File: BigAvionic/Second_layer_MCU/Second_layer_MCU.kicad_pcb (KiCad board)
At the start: 4 copper layers, 68 x 68 mm, 89 parts, among them J1 Conn_01x02, J10 Conn_01x04, J12 Conn_01x04, J2 USB_C_Receptacle_USB2.0_16P, J3 Conn_01x04, J6 Micro_SD_Card_Det1, J7 Screw_Terminal_01x01, J9 Conn_01x04, Q5 NMOS, SW1 SW_Push, SW2 USER_Buttom, SW3 USER_Buttom, U1 STM32F405VGTx, U12 W25Q128JVS, U5 BMI088, U6 BMP390, U8 ADXL375BCCZ, Y1 8Mhz

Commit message: finish power layer(still need check)
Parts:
- removed J7: Screw_Terminal_01x01, TerminalBlock_Phoenix:TerminalBlock_Phoenix_PT-1,5-2-3.5-H_1x02_P3.50mm_Horizontal
- removed R10: 0 ohm, Resistor_SMD:R_0805_2012Metric_Pad1.20x1.40mm_HandSolder
- removed R5, R54: 0ohm, Resistor_SMD:R_0805_2012Metric_Pad1.20x1.40mm_HandSolder
- added J4: Screw_Terminal_01x02, TerminalBlock_Phoenix:TerminalBlock_Phoenix_PT-1,5-2-3.5-H_1x02_P3.50mm_Horizontal, F.Cu at (86.1, 67.9)
- C1, C11, C2, C20, C25, C26, C27, C28, C29, C3, C30, C31, C32, C36, C37, C4, C48, C5, C50, C51, C53, C6, C7, C8, C9: footprint Capacitor_SMD:C_0805_2012Metric_Pad1.18x1.45mm_HandSolder -> Capacitor_SMD:C_0603_1608Metric_Pad1.08x0.95mm_HandSolder
- R35, R38, R40, R41, R44: value 47k -> 10k
- Y1: footprint Crystal:Crystal_HC49-U_Vertical -> Crystal:Crystal_SMD_5032-4Pin_5.0x3.2mm
- moved U1 91.3 mm to (130.5, 120.0)
- moved D11 62.0 mm to (84.0, 33.5)
- moved D12 62.0 mm to (84.0, 36.6)
- moved D5 62.0 mm to (84.0, 27.4)
- moved BZ1 62.0 mm to (71.0, 32.7)
- moved D8 62.0 mm to (84.0, 30.5)
- moved U6 48.8 mm to (43.5, 81.6)
- moved Q5 48.8 mm to (38.9, 81.7)
- moved U5 48.8 mm to (33.4, 82.2)
- moved J12 47.0 mm to (33.8, 76.2)
- moved J6 27.4 mm to (68.4, 73.2)
- moved U12 26.4 mm to (82.0, 78.6)
- moved C11 23.3 mm to (37.5, 33.4)
- moved C27 23.3 mm to (37.5, 45.5)
- moved C3 23.3 mm to (32.6, 33.4)
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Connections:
- C28 pad 1: Net-(C28-Pad1) -> HSE_OUT
- J2 pad A6: Net-(J2-D+-PadA6) -> USB_D+
- J2 pad A7: Net-(J2-D--PadA7) -> USB_D-
- J2 pad B6: Net-(J2-D+-PadA6) -> USB_D+
- J2 pad B7: Net-(J2-D--PadA7) -> USB_D-
- R39 pad 2: SDIO_CK -> SDIO_CMD

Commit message: add lora files
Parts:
- added J5: Conn_01x08, Connector_JST:JST_GH_SM08B-GHS-TB_1x08-1MP_P1.25mm_Horizontal, B.Cu at (160.5, 110.0)
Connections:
- net +USB_5V renamed Net-(J2-VBUS-PadA4)
- U1 pad 16: unconnected-(U1-PC1-Pad16) -> SUP_STAT
- U1 pad 17: unconnected-(U1-PC2-Pad17) -> PG_BUCK

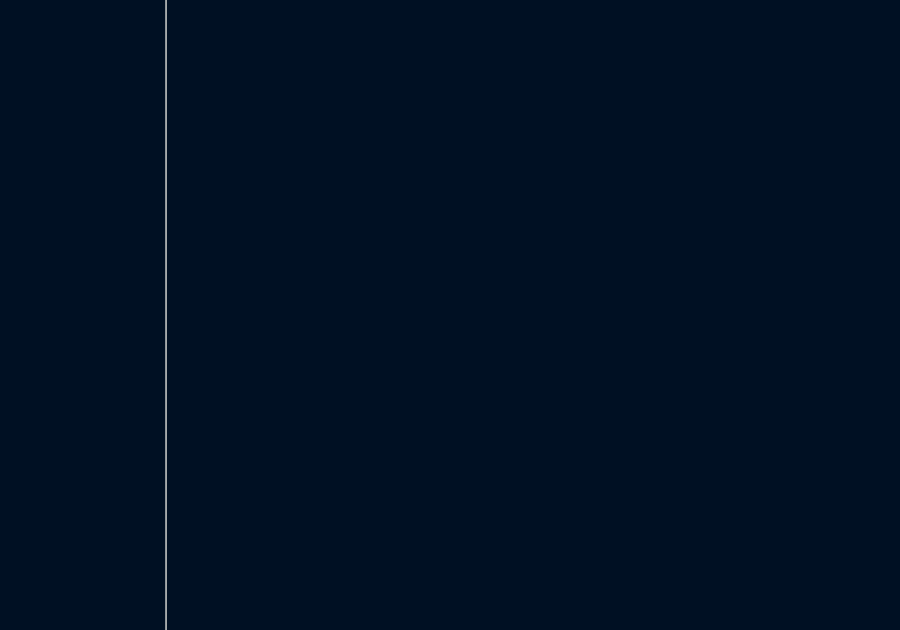
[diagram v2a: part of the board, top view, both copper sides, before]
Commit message: add new power layer
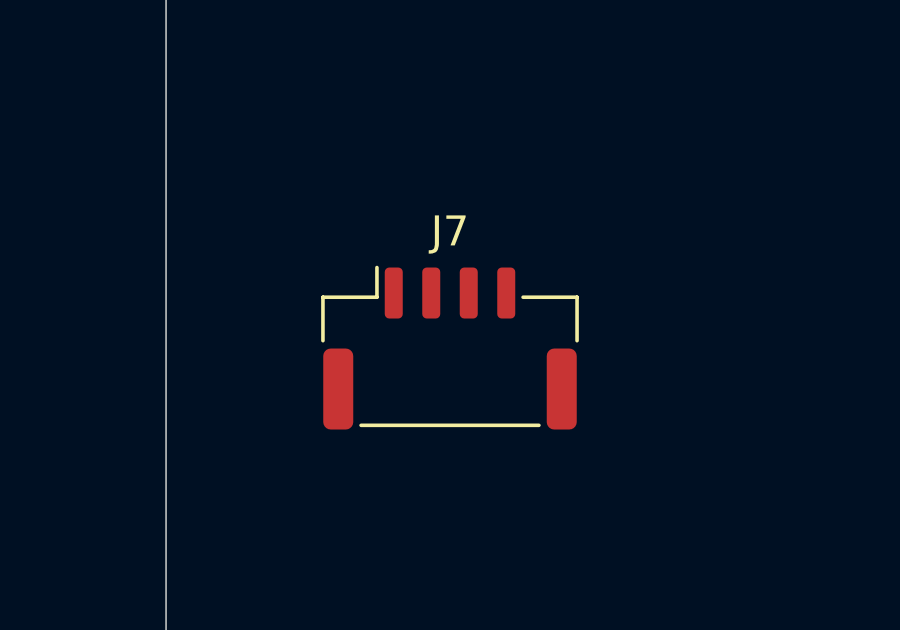
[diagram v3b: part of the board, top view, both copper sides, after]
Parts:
- added J7: Conn_01x04, Connector_JST:JST_GH_SM04B-GHS-TB_1x04-1MP_P1.25mm_Horizontal, F.Cu at (106.0, 123.8)

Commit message: MCU process
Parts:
- removed Q5: NMOS, Package_TO_SOT_SMD:SOT-23
- removed the R27 at (37.4, 54.4)
- removed R34, R36, R37, R39, R42, R43: 22ohm, Resistor_SMD:R_0805_2012Metric_Pad1.20x1.40mm_HandSolder
- added C30: 22u, Capacitor_SMD:C_1206_3216Metric_Pad1.33x1.80mm_HandSolder, B.Cu at (154.5, 110.1)
- added C31: 22u, Capacitor_SMD:C_1206_3216Metric_Pad1.33x1.80mm_HandSolder, B.Cu at (150.8, 110.1)
- added J11: Conn_01x04, Connector_JST:JST_GH_SM04B-GHS-TB_1x04-1MP_P1.25mm_Horizontal, B.Cu at (160.5, 110.1)
- added J13: Conn_01x08, Connector_JST:JST_GH_SM08B-GHS-TB_1x08-1MP_P1.25mm_Horizontal, F.Cu at (120.5, 90.0)
- added J14: Conn_01x08, Connector_JST:JST_GH_SM08B-GHS-TB_1x08-1MP_P1.25mm_Horizontal, F.Cu at (140.5, 90.0)
- added Q2: BSS138, Package_TO_SOT_SMD:SOT-23, F.Cu at (131.3, 78.5)
- added R1: 100k, Resistor_SMD:R_0402_1005Metric_Pad0.72x0.64mm_HandSolder, F.Cu at (125.0, 67.5)
- added R17: 22ohm, Resistor_SMD:R_0402_1005Metric_Pad0.72x0.64mm_HandSolder, F.Cu at (141.3, 124.0)
- added R19: 22ohm, Resistor_SMD:R_0402_1005Metric_Pad0.72x0.64mm_HandSolder, F.Cu at (133.2, 109.4)
- added R32: 22ohm, Resistor_SMD:R_0402_1005Metric_Pad0.72x0.64mm_HandSolder, F.Cu at (133.7, 70.0)
- added R33: 22ohm, Resistor_SMD:R_0402_1005Metric_Pad0.72x0.64mm_HandSolder, B.Cu at (133.1, 109.4)
- added R35: 10k, Resistor_SMD:R_0402_1005Metric_Pad0.72x0.64mm_HandSolder, F.Cu at (107.8, 132.6)
- added R4: 4.7k, Resistor_SMD:R_0402_1005Metric_Pad0.72x0.64mm_HandSolder, F.Cu at (125.0, 70.0)
- added R5: 4.7k, Resistor_SMD:R_0402_1005Metric_Pad0.72x0.64mm_HandSolder, F.Cu at (125.0, 72.5)
- added R6: 22ohm, Resistor_SMD:R_0402_1005Metric_Pad0.72x0.64mm_HandSolder, F.Cu at (141.4, 119.0)
- added R7: 22ohm, Resistor_SMD:R_0402_1005Metric_Pad0.72x0.64mm_HandSolder, F.Cu at (141.3, 117.8)
- added R8: 22ohm, Resistor_SMD:R_0402_1005Metric_Pad0.72x0.64mm_HandSolder, F.Cu at (135.6, 109.4)
- added R9: 22ohm, Resistor_SMD:R_0402_1005Metric_Pad0.72x0.64mm_HandSolder, F.Cu at (134.4, 109.4)
- BZ1: footprint Buzzer_Beeper:Buzzer_12x9.5RM7.6 -> Buzzer_Beeper:MagneticBuzzer_CUI_CMT-8504-100-SMT
- C10: renamed from C8; footprint Capacitor_SMD:C_0603_1608Metric_Pad1.08x0.95mm_HandSolder -> Capacitor_SMD:C_0402_1005Metric_Pad0.74x0.62mm_HandSolder
- C11: renamed from C9; footprint Capacitor_SMD:C_0603_1608Metric_Pad1.08x0.95mm_HandSolder -> Capacitor_SMD:C_0402_1005Metric_Pad0.74x0.62mm_HandSolder
- C13: renamed from C48; footprint Capacitor_SMD:C_0603_1608Metric_Pad1.08x0.95mm_HandSolder -> Capacitor_SMD:C_0402_1005Metric_Pad0.74x0.62mm_HandSolder
- C14: renamed from C20; footprint Capacitor_SMD:C_0603_1608Metric_Pad1.08x0.95mm_HandSolder -> Capacitor_SMD:C_0402_1005Metric_Pad0.74x0.62mm_HandSolder
- C15: renamed from C25; footprint Capacitor_SMD:C_0603_1608Metric_Pad1.08x0.95mm_HandSolder -> Capacitor_SMD:C_0402_1005Metric_Pad0.74x0.62mm_HandSolder
- C16: renamed from C11; footprint Capacitor_SMD:C_0603_1608Metric_Pad1.08x0.95mm_HandSolder -> Capacitor_SMD:C_0402_1005Metric_Pad0.74x0.62mm_HandSolder
- C2: renamed from C3; footprint Capacitor_SMD:C_0603_1608Metric_Pad1.08x0.95mm_HandSolder -> Capacitor_SMD:C_0402_1005Metric_Pad0.74x0.62mm_HandSolder
- C20: renamed from C36; footprint Capacitor_SMD:C_0603_1608Metric_Pad1.08x0.95mm_HandSolder -> Capacitor_SMD:C_0402_1005Metric_Pad0.74x0.62mm_HandSolder
- C22: renamed from C37; footprint Capacitor_SMD:C_0603_1608Metric_Pad1.08x0.95mm_HandSolder -> Capacitor_SMD:C_0402_1005Metric_Pad0.74x0.62mm_HandSolder
- C23: renamed from C29; footprint Capacitor_SMD:C_0603_1608Metric_Pad1.08x0.95mm_HandSolder -> Capacitor_SMD:C_0402_1005Metric_Pad0.74x0.62mm_HandSolder
- C24: renamed from C50; footprint Capacitor_SMD:C_0603_1608Metric_Pad1.08x0.95mm_HandSolder -> Capacitor_SMD:C_0402_1005Metric_Pad0.74x0.62mm_HandSolder
- C25: renamed from C30; footprint Capacitor_SMD:C_0603_1608Metric_Pad1.08x0.95mm_HandSolder -> Capacitor_SMD:C_0402_1005Metric_Pad0.74x0.62mm_HandSolder
- C26: renamed from C31; footprint Capacitor_SMD:C_0603_1608Metric_Pad1.08x0.95mm_HandSolder -> Capacitor_SMD:C_0402_1005Metric_Pad0.74x0.62mm_HandSolder
- C27: renamed from C32; footprint Capacitor_SMD:C_0603_1608Metric_Pad1.08x0.95mm_HandSolder -> Capacitor_SMD:C_0402_1005Metric_Pad0.74x0.62mm_HandSolder
- C28: renamed from C51; footprint Capacitor_SMD:C_0603_1608Metric_Pad1.08x0.95mm_HandSolder -> Capacitor_SMD:C_0402_1005Metric_Pad0.74x0.62mm_HandSolder
- C29: renamed from C53; footprint Capacitor_SMD:C_0603_1608Metric_Pad1.08x0.95mm_HandSolder -> Capacitor_SMD:C_0402_1005Metric_Pad0.74x0.62mm_HandSolder
- C3: renamed from C26; footprint Capacitor_SMD:C_0603_1608Metric_Pad1.08x0.95mm_HandSolder -> Capacitor_SMD:C_0402_1005Metric_Pad0.74x0.62mm_HandSolder
- C4, C5, C6, C7: footprint Capacitor_SMD:C_0603_1608Metric_Pad1.08x0.95mm_HandSolder -> Capacitor_SMD:C_0402_1005Metric_Pad0.74x0.62mm_HandSolder
- D4: renamed from D12; footprint LED_SMD:LED_0805_2012Metric_Pad1.15x1.40mm_HandSolder -> Diode_SMD:D_SOD-123
- J10: renamed from J7; moved to B.Cu
- J4: renamed from J6; footprint Connector_Card:microSD_HC_Molex_47219-2001 -> Connector_Card:microSD_HC_Molex_104031-0811
- J5: renamed from J10; footprint Connector_JST:JST_EH_S4B-EH_1x04_P2.50mm_Horizontal -> Connector_JST:JST_GH_SM04B-GHS-TB_1x04-1MP_P1.25mm_Horizontal
- J6: renamed from J12; footprint Connector_JST:JST_EH_B4B-EH-A_1x04_P2.50mm_Vertical -> Connector_PinHeader_2.54mm:PinHeader_1x04_P2.54mm_Vertical
- J8: renamed from J9; footprint Connector_JST:JST_EH_S4B-EH_1x04_P2.50mm_Horizontal -> Connector_JST:JST_GH_SM04B-GHS-TB_1x04-1MP_P1.25mm_Horizontal
- J9: renamed from J5; moved to F.Cu
- R10: renamed from R44; footprint Resistor_SMD:R_0805_2012Metric_Pad1.20x1.40mm_HandSolder -> Resistor_SMD:R_0402_1005Metric_Pad0.72x0.64mm_HandSolder; moved to B.Cu
- R11: renamed from R40; footprint Resistor_SMD:R_0805_2012Metric_Pad1.20x1.40mm_HandSolder -> Resistor_SMD:R_0402_1005Metric_Pad0.72x0.64mm_HandSolder; moved to B.Cu
- R12: renamed from R9; footprint Resistor_SMD:R_0805_2012Metric_Pad1.20x1.40mm_HandSolder -> Resistor_SMD:R_0402_1005Metric_Pad0.72x0.64mm_HandSolder
- R13: renamed from R38; footprint Resistor_SMD:R_0805_2012Metric_Pad1.20x1.40mm_HandSolder -> Resistor_SMD:R_0402_1005Metric_Pad0.72x0.64mm_HandSolder; moved to B.Cu
- R14: renamed from R41; footprint Resistor_SMD:R_0805_2012Metric_Pad1.20x1.40mm_HandSolder -> Resistor_SMD:R_0402_1005Metric_Pad0.72x0.64mm_HandSolder; moved to B.Cu
- R15: renamed from R35; footprint Resistor_SMD:R_0805_2012Metric_Pad1.20x1.40mm_HandSolder -> Resistor_SMD:R_0402_1005Metric_Pad0.72x0.64mm_HandSolder; moved to B.Cu
- R16: renamed from R3; footprint Resistor_SMD:R_0805_2012Metric_Pad1.20x1.40mm_HandSolder -> Resistor_SMD:R_0402_1005Metric_Pad0.72x0.64mm_HandSolder
- R18: renamed from R4; footprint Resistor_SMD:R_0805_2012Metric_Pad1.20x1.40mm_HandSolder -> Resistor_SMD:R_0402_1005Metric_Pad0.72x0.64mm_HandSolder
- R2: renamed from R6; footprint Resistor_SMD:R_0805_2012Metric_Pad1.20x1.40mm_HandSolder -> Resistor_SMD:R_0402_1005Metric_Pad0.72x0.64mm_HandSolder
- R20: renamed from R45; footprint Resistor_SMD:R_0805_2012Metric_Pad1.20x1.40mm_HandSolder -> Resistor_SMD:R_0402_1005Metric_Pad0.72x0.64mm_HandSolder
- R21: renamed from R46; footprint Resistor_SMD:R_0805_2012Metric_Pad1.20x1.40mm_HandSolder -> Resistor_SMD:R_0402_1005Metric_Pad0.72x0.64mm_HandSolder
- R22: renamed from R47; footprint Resistor_SMD:R_0805_2012Metric_Pad1.20x1.40mm_HandSolder -> Resistor_SMD:R_0402_1005Metric_Pad0.72x0.64mm_HandSolder
- R23: footprint Resistor_SMD:R_0805_2012Metric_Pad1.20x1.40mm_HandSolder -> Resistor_SMD:R_0402_1005Metric_Pad0.72x0.64mm_HandSolder
- R24: renamed from R8; footprint Resistor_SMD:R_0805_2012Metric_Pad1.20x1.40mm_HandSolder -> Resistor_SMD:R_0402_1005Metric_Pad0.72x0.64mm_HandSolder
- R25: renamed from R22; footprint Resistor_SMD:R_0805_2012Metric_Pad1.20x1.40mm_HandSolder -> Resistor_SMD:R_0402_1005Metric_Pad0.72x0.64mm_HandSolder
- R26: renamed from R28; footprint Resistor_SMD:R_0805_2012Metric_Pad1.20x1.40mm_HandSolder -> Resistor_SMD:R_0402_1005Metric_Pad0.72x0.64mm_HandSolder
- R27: renamed from R48; footprint Resistor_SMD:R_0805_2012Metric_Pad1.20x1.40mm_HandSolder -> Resistor_SMD:R_0402_1005Metric_Pad0.72x0.64mm_HandSolder
- R28: renamed from R49; footprint Resistor_SMD:R_0805_2012Metric_Pad1.20x1.40mm_HandSolder -> Resistor_SMD:R_0402_1005Metric_Pad0.72x0.64mm_HandSolder
- R29: renamed from R53; footprint Resistor_SMD:R_0805_2012Metric_Pad1.20x1.40mm_HandSolder -> Resistor_SMD:R_0402_1005Metric_Pad0.72x0.64mm_HandSolder
- R3: renamed from R7; footprint Resistor_SMD:R_0805_2012Metric_Pad1.20x1.40mm_HandSolder -> Resistor_SMD:R_0402_1005Metric_Pad0.72x0.64mm_HandSolder
- R30: renamed from R50; footprint Resistor_SMD:R_0805_2012Metric_Pad1.20x1.40mm_HandSolder -> Resistor_SMD:R_0402_1005Metric_Pad0.72x0.64mm_HandSolder
- R31: renamed from R51; footprint Resistor_SMD:R_0805_2012Metric_Pad1.20x1.40mm_HandSolder -> Resistor_SMD:R_0402_1005Metric_Pad0.72x0.64mm_HandSolder
- Y1: footprint Crystal:Crystal_SMD_5032-4Pin_5.0x3.2mm -> Crystal:Crystal_SMD_3225-4Pin_3.2x2.5mm_HandSoldering
- moved C11 142.5 mm to (138.3, 128.1)
- moved C5 130.7 mm to (140.2, 113.8), turned to -90 degrees
- moved C6 127.1 mm to (125.2, 129.6), turned to 180 degrees
- moved C2 122.3 mm to (120.2, 118.7), turned to 180 degrees
- moved J1 120.7 mm to (170.5, 94.3)
- moved C16 119.4 mm to (116.1, 123.2), turned to 90 degrees
- moved C14 119.1 mm to (119.1, 123.2), turned to 90 degrees
- moved C1 118.1 mm to (118.9, 116.0), turned to -90 degrees
- moved J5 118.1 mm to (160.5, 130.0), turned to 90 degrees
- moved C4 117.8 mm to (124.5, 110.2)
- moved C7 117.4 mm to (120.6, 123.2), turned to -90 degrees
- moved R15 116.7 mm to (146.0, 105.8)
- moved C15 115.9 mm to (117.6, 123.2), turned to 90 degrees
- moved R11 114.0 mm to (145.4, 102.8), turned to 90 degrees
- moved R13 113.4 mm to (146.0, 104.6)
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- renumbered C10 to C1, C47 to C12, C27 to C17, C28 to C18, C38 to C19, C49 to C21, C2 to C8, C1 to C9, D8 to D1, D11 to D2, D5 to D3, J3 to J1, J1 to J3, J4 to J7, U12 to U2, U8 to U3, U6 to U4
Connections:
- BZ1 pad 1: V_BAT+ -> +3.3V
- C1 pad 1: +3V3 -> +3.3V
- C10 pad 1: +3V3 -> +3.3V
- C11 pad 1: +3V3 -> +3.3V
- C2 pad 1: +3V3 -> +3.3V
- C4 pad 1: +3V3 -> +3.3V
- C5 pad 1: +3V3 -> +3.3V
- C6 pad 1: +3V3 -> +3.3V
- C7 pad 1: +3V3 -> +3.3V
- D4 pad 1: V_BAT+ -> +3.3V
- FB1 pad 2: +3V3 -> +3.3V
- J10 pad 1: Battery_Sensing -> GND
- J10 pad 2: SUP_STAT -> GND
- J10 pad 3: PG_BUCK -> SUP_STAT
- J10 pad 4: GND -> Battery_Sensing
- J4 pad 1: Net-(J6-DAT2) -> SDIO_D2
- J4 pad 2: Net-(J6-DAT3/CD) -> SDIO_D3
- J4 pad 3: Net-(J6-CMD) -> SDIO_CMD
- J4 pad 5: Net-(J6-CLK) -> SDIO_CK
- J4 pad 7: Net-(J6-DAT0) -> SDIO_D0
- J4 pad 8: Net-(J6-DAT0) -> SDIO_D1
- R10 pad 1: Net-(J6-DAT0) -> SDIO_D0
- R11 pad 1: Net-(J6-CMD) -> SDIO_CMD
- R13 pad 1: Net-(J6-DAT3/CD) -> SDIO_D3
- R14 pad 1: Net-(J6-DAT0) -> SDIO_D1
- R15 pad 1: Net-(J6-DAT2) -> SDIO_D2
- U1 pad 100: +3V3 -> +3.3V
- U1 pad 11: +3V3 -> +3.3V
- U1 pad 19: +3V3 -> +3.3V
- U1 pad 28: +3V3 -> +3.3V
- U1 pad 50: +3V3 -> +3.3V
- U1 pad 55: UART3_TX -> Net-(U1-PD8)
- U1 pad 6: +3V3 -> +3.3V
- U1 pad 63: UART6_TX -> Net-(U1-PC6)
- U1 pad 64: Net-(U1-PC7) -> UART6_RX
- U1 pad 65: SDIO_D0 -> Net-(U1-PC8)
- U1 pad 66: SDIO_D1 -> Net-(U1-PC9)
- U1 pad 75: +3V3 -> +3.3V
- U1 pad 78: SDIO_D2 -> Net-(U1-PC10)
- U1 pad 79: SDIO_D3 -> Net-(U1-PC11)
- U1 pad 80: SDIO_CK -> Net-(U1-PC12)
- U1 pad 83: SDIO_CMD -> Net-(U1-PD2)
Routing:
- net SDIO_DET: track 0.00 -> 37.2 mm
- net GND: track 0.00 -> 29.3 mm, vias 0 -> 12
- net SDIO_D0: track 0.00 -> 25.2 mm, vias 0 -> 1
- net SDIO_D1: track 0.00 -> 24.7 mm, vias 0 -> 3
- net +3.3V: track 0.00 -> 19.7 mm, vias 0 -> 8
- net SDIO_CMD: track 0.00 -> 14.6 mm, vias 0 -> 2
- net SDIO_CK: track 0.00 -> 13.3 mm
- net HSE_OUT: track 0.00 -> 13.1 mm
- net HSE_IN: track 0.00 -> 13.0 mm
- net SDIO_D3: track 0.00 -> 12.8 mm, vias 0 -> 1
- net SDIO_D2: track 0.00 -> 11.1 mm, vias 0 -> 1
- net VREF: track 0.00 -> 9.63 mm
- net Net-(U1-PC9): track 0.00 -> 2.87 mm
- net Net-(U1-PC12): track 0.00 -> 2.84 mm
- net Net-(U1-PC11): track 0.00 -> 2.62 mm
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- added copper zone on B.Cu, net +3.3V
- added copper zone on In2.Cu, net +3.3V
- added copper zone on B.Cu, net GND
- added copper zone on F.Cu, net GND
- added copper zone on In1.Cu, net GND
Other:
- board text added: "P_MCU"
- board text added: "S_L433"
- board text added: "S_L920"
- board text added: "S_MCU"

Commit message: MCU layer progress 1
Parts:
- C21, C24, C25, C27, R20, R21, R22, R23, R25, U2, U5: moved to B.Cu
- moved C23 135.8 mm to (124.3, 135.6), turned to -90 degrees
- moved C26 130.5 mm to (122.3, 136.4), turned to 180 degrees
- moved C22 130.3 mm to (131.6, 137.2), turned to 180 degrees
- moved C20 130.2 mm to (128.2, 137.2)
- moved C19 129.7 mm to (131.1, 139.9), turned to 180 degrees
- moved C25 124.0 mm to (131.4, 116.7), turned to 90 degrees
- moved C27 123.3 mm to (129.1, 124.0), turned to -90 degrees
- moved R24 122.3 mm to (133.9, 134.8), turned to 90 degrees
- moved R23 112.2 mm to (129.0, 116.1), turned to 180 degrees
- moved R26 111.1 mm to (120.5, 131.1), turned to -90 degrees
- moved R25 110.9 mm to (130.5, 124.4), turned to 90 degrees
- moved U5 104.2 mm to (130.5, 120.0), turned to 180 degrees
- moved C21 102.8 mm to (125.1, 97.4), turned to 180 degrees
- moved C24 102.7 mm to (125.6, 99.7), turned to 180 degrees
- moved R22 101.6 mm to (135.8, 100.6), turned to 90 degrees
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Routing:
- net +3.3V: track 19.7 -> 75.0 mm, vias 8 -> 28
- net GND: track 29.3 -> 67.5 mm, vias 12 -> 35
- net SPI3_SCK: track 0.00 -> 33.7 mm, vias 0 -> 2
- net SPI3_MOSI: track 0.00 -> 33.2 mm, vias 0 -> 2
- net LORA920_RST: track 0.00 -> 28.8 mm, vias 0 -> 2
- net CSB_Gyro: track 0.00 -> 27.0 mm, vias 0 -> 1
- net SPI3_MISO: track 0.00 -> 26.6 mm, vias 0 -> 2
- net LORA920_INT: track 0.00 -> 24.8 mm
- net CSB_LORA920: track 0.00 -> 23.3 mm
- net LORA920_BUSY: track 0.00 -> 23.1 mm, vias 0 -> 2
- net CSB_Flash: track 0.00 -> 19.2 mm, vias 0 -> 1
- net INT_Baro: track 0.00 -> 17.4 mm
- net INT_Accel2: track 0.00 -> 16.6 mm, vias 0 -> 1
- net SPI1_SCK: track 0.00 -> 16.5 mm
- net SPI2_MOSI: track 0.00 -> 15.7 mm, vias 0 -> 1
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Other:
- board text added: "X"
- board text added: "Y"
- board text added: "Z"

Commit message: finish all layer
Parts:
- C12, C13, J5: moved to B.Cu
- C8, C9: footprint Capacitor_SMD:C_0603_1608Metric_Pad1.08x0.95mm_HandSolder -> Capacitor_SMD:C_0805_2012Metric_Pad1.18x1.45mm_HandSolder
- R27, R28, R29: footprint Resistor_SMD:R_0402_1005Metric_Pad0.72x0.64mm_HandSolder -> Resistor_SMD:R_0603_1608Metric_Pad0.98x0.95mm_HandSolder
- SW2, SW3: footprint Button_Switch_THT:SW_PUSH_6mm_H4.3mm -> Button_Switch_SMD:SW_Push_1P1T-SH_NO_CK_KMR2xxG
- moved C8 146.4 mm to (137.8, 132.2), turned to -90 degrees
- moved R3 141.4 mm to (151.0, 140.6)
- moved R2 140.4 mm to (147.0, 141.7), turned to 90 degrees
- moved C9 139.0 mm to (143.0, 112.0)
- moved R12 133.9 mm to (145.2, 141.7), turned to -90 degrees
- moved BZ1 129.5 mm to (131.5, 147.2)
- moved R18 129.4 mm to (135.5, 132.9), turned to -90 degrees
- moved C13 122.2 mm to (142.7, 103.6)
- moved J2 119.7 mm to (148.5, 148.8)
- moved C3 118.0 mm to (116.2, 130.3), turned to -90 degrees
- moved D4 117.6 mm to (124.0, 147.1), turned to -90 degrees
- moved C12 117.6 mm to (143.8, 107.7)
- moved R31 110.2 mm to (125.5, 140.5)
- moved R16 109.5 mm to (126.9, 107.2), turned to 180 degrees
- moved C28 109.4 mm to (110.6, 125.5), turned to 90 degrees
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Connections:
- U1 pad 17: PG_BUCK -> unconnected-(U1-PC2-Pad17)
- U1 pad 42: unconnected-(U1-PE11-Pad42) -> LORA433_BUSY
- U1 pad 43: unconnected-(U1-PE12-Pad43) -> INT_Magn
- U1 pad 67: unconnected-(U1-PA8-Pad67) -> RST_GPS
- U1 pad 69: RST_GPS -> unconnected-(U1-PA10-Pad69)
- U1 pad 92: INT_Magn -> unconnected-(U1-PB6-Pad92)
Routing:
- net I2C1_SDA: track 0.00 -> 67.1 mm, vias 0 -> 4
- net I2C1_SCL: track 0.00 -> 64.8 mm, vias 0 -> 5
- net LORA433_M1: track 0.00 -> 58.6 mm, vias 0 -> 2
- net LORA433_BUSY: track 0.00 -> 53.0 mm, vias 0 -> 2
- net +3.3V: track 75.0 -> 122.5 mm, vias 28 -> 46
- net UART3_RX: track 0.00 -> 43.0 mm, vias 0 -> 2
- net LORA433_M0: track 0.00 -> 42.9 mm
- net UART3_TX: track 0.00 -> 42.7 mm, vias 0 -> 2
- net RESET: track 0.00 -> 42.0 mm, vias 0 -> 2
- net LORA433_RST: track 0.00 -> 41.8 mm
- net USB_D+: track 0.00 -> 41.6 mm, vias 0 -> 2
- net USB_D-: track 0.00 -> 39.9 mm, vias 0 -> 3
- net INT_Magn: track 0.00 -> 39.0 mm, vias 0 -> 2
- net UART6_RX: track 0.00 -> 35.2 mm, vias 0 -> 2
- net USB_VBUS: track 0.00 -> 27.8 mm, vias 0 -> 2
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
